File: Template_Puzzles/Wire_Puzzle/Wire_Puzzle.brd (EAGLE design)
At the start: 44.4 x 42.9 mm, 24 parts, among them Q1 2N7002

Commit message: Wire_Puzzle progress
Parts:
- removed J0, J1, J2, J3, J4, J5, J6, J7: (no value), SparkFun-Connectors:1X04
- added D1: 1N4001, Diodes:DO-41
- added IC1: 7805T, linear:TO220H
- added R3: 330R, Resistor:RESAD724W46L381D178B
- added U$10, U$11, U$12, U$13, U$14, U$15, U$16, U$17: 1X02, Adam's Parts (work):1X02
- added U$18, U$19, U$20, U$21, U$22, U$23, U$24, U$25, U$26, U$27: 1X03, Adam's Parts (work):1X03
- FRAME1: value FRAME-LETTER -> FRAME-LEDGER
- Q1: value 2N7002 -> 2N7000
- moved U$9 176.1 mm to (79.0, 47.0)
- moved R2 157.9 mm to (36.0, 58.0), turned to 90 degrees
- moved R1 155.8 mm to (40.4, 58.1), turned to 90 degrees
- moved LED2 150.6 mm to (36.0, 67.0), turned to 270 degrees
- moved LED1 143.9 mm to (17.0, 81.0), turned to 180 degrees
- moved Q1 142.0 mm to (36.0, 50.0), turned to 270 degrees
- moved U$5 139.2 mm to (81.0, 56.0), turned to 90 degrees
- moved U$8 112.8 mm to (8.00, 52.0)
- moved U$4 110.9 mm to (69.0, 43.0), turned to 180 degrees
- moved U$7 105.4 mm to (32.0, 36.0)
- moved U$6 101.1 mm to (23.0, 52.0), turned to 180 degrees
- moved U$2 54.3 mm to (8.01, 79.2), turned to 0 degrees
- moved FRAME1 28.8 mm to (-47.0, -114.0)
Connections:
- new net 3V_1: U$4.P$5
- new net 3V_2: U$4.P$17
- new net 3V_3: U$4.P$26
- new net G_2: U$4.P$6
- new net G_4: U$4.P$18
- new net N$5: LED1.A, R3.2
- new net VU: U$4.P$13
- net 5V: now also D1.C, IC1.3, R3.1, U$18.2, U$19.2, U$20.2, U$21.2, U$22.2, U$23.2, U$24.2, U$25.2, U$26.2, U$27.2
- net A: now also U$10.2; no longer J0.2
- net A0: now also U$27.3
- net B: now also U$11.2; no longer J1.2
- net C: now also U$12.2; no longer J2.2
- net D: now also U$13.2; no longer J3.2
- net D0: now also U$18.3, U$7.2
- net D1: now also U$19.3
- net D2: now also U$20.3, U$3.14; no longer U$7.2
- net D3: now also U$21.3
- net D4: now also U$22.3
- net D5: now also U$23.3
- net D6: now also U$24.3
- net D7: now also U$25.3; no longer U$3.14
- net D8: now also U$26.3
- net E: now also U$14.2; no longer J4.2
- net F: now also U$15.2; no longer J5.2
- net G: now also U$16.2; no longer J6.2
- net GND: now also IC1.2, LED1.K, U$18.1, U$19.1, U$20.1, U$21.1, U$22.1, U$23.1, U$24.1, U$25.1, U$26.1, U$27.1; no longer J0.3, J0.4, J1.3, J1.4, J2.3, J2.4, J3.3, J3.4, J4.3, J4.4, J5.3, J5.4, J6.3, J6.4, J7.3, J7.4
- net H: now also U$17.2; no longer J7.2
- net N$4: now also D1.A
- net QA: now also U$10.1; no longer J0.1
- net QB: now also U$11.1; no longer J1.1
- net QC: now also U$12.1; no longer J2.1
- net QD: now also U$13.1; no longer J3.1
- net QE: now also U$14.1; no longer J4.1
- net QF: now also U$15.1; no longer J5.1
- net QG: now also U$16.1; no longer J6.1
- net QH: now also U$17.1; no longer J7.1
- net VCC: now also IC1.1
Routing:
- net D1: track 0.00 -> 60.1 mm, vias 0 -> 2
- net A0: track 0.00 -> 45.0 mm
- net D8: track 0.00 -> 43.6 mm, vias 0 -> 1
- net D2: track 0.00 -> 36.8 mm
- net N$4: track 0.00 -> 32.3 mm
- net N$1: track 0.00 -> 23.1 mm
- net VCC: track 0.00 -> 19.1 mm
- net D7: track 30.4 -> 47.7 mm, vias 0 -> 1
- net D6: track 21.2 -> 34.4 mm, vias 0 -> 1
- net D3: track 39.5 -> 52.5 mm, vias 0 -> 1
- net N$8: track 0.00 -> 12.7 mm
- net N$3: track 0.00 -> 9.31 mm
- net N$2: track 0.00 -> 9.31 mm
- net 5V: track 17.4 -> 25.3 mm
- net N$7: track 0.00 -> 7.20 mm
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- removed copper zone on layer 1, net GND
- removed copper zone on layer 16, net GND
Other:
- board size 44.4 x 42.9 mm -> 88.4 x 90.8 mm
- board text added: "+"
- board text added: "+12"
- board text added: "A0"
- board text added: "COM"
- board text added: "D0"
- board text added: "D1"
- board text added: "D2"
- board text added: "D3"
- board text added: "D4"
- board text added: "D5"
- board text added: "D6"
- board text added: "D7"
- board text added: "D8"
- board text added: "G 5V S"
- board text added: "NC"
- board text added: "NO"
- board text added: "PUZZLE WIRES"
- board text added: "_"
- board text removed: "5V"
- board text removed: "BTN-"
- board text removed: "LED-"
- board text removed: "WIRE+"
- board text removed: "WIRE-"

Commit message: Progress, added audio amp, power
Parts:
- added C1: 1000uF, adafruit:E5-10,5
- added C2: 100uF, adafruit:E5-10,5
- added C3: 0.1uF, capacitor-wima:C2.5-2
- added C4: 0.33uF, rcl:E2-5
- added C5: 0.1uF, rcl:E2-5
- added D2: 1N4001, Diodes:DO-41
- added R4, R5: 1K, Resistor:RESAD724W46L381D178B
- added R6: 10R, Resistor:RESAD724W46L381D178B
- added S1: (no value), Adam's Parts (work):SWITCH_SLIDING_SSP1S1
- added U1: LM386N, SparkFun-IC-Amplifiers:DIP08
- added VR1: 10k, SparkFun-Resistors:TRIMPOT-PTH-3386U
- R2: value (none) -> 330R
- moved LED1 99.2 mm to (114.0, 60.0), turned to 0 degrees
- moved R3 85.7 mm to (107.8, 63.6), turned to 270 degrees
- moved U$9 73.4 mm to (8.00, 65.7), turned to 180 degrees
- moved IC1 20.6 mm to (27.0, 77.0), turned to 270 degrees
- moved U$2 2.50 mm to (7.99, 76.8), turned to 180 degrees
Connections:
- new net AUDIO: R4.1, R5.1, VR1.2
- new net N$10: C3.2, R6.1
- new net N$11: R5.2, U$5.P$13
- new net N$12: U1.3, VR1.3
- new net N$13: S1.2, U$2.2
- new net N$14: C2.+, U1.7
- new net N$9: C1.-, U$9.1
- net 5V: now also C5.+, D2.A
- net GND: now also C2.-, C4.-, C5.-, R6.2, U$9.2, U1.2, U1.4
- net N$7: now also C1.+, C3.1, U1.5; no longer U$5.P$16, U$9.1
- net N$8: now also R4.2, U$5.P$12; no longer U$5.P$14, U$9.2
- net VCC: now also C4.+, D2.C, S1.3, U1.6; no longer U$2.2
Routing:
- net VCC: track 19.1 -> 0.08 mm
- net N$8: track 12.7 -> 0.00 mm
- net N$4: track 32.3 -> 23.2 mm
- net N$7: track 7.20 -> 0.00 mm
- net 5V: track 25.3 -> 21.8 mm
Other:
- board text added: "SPKR"

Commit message: Finished wire puzzle
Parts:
- R2, R3: value 330R -> 330
- R6: value 10R -> 10
- moved S1 298.2 mm to (9.90, 86.0)
- moved D2 282.0 mm to (14.6, 76.7), turned to 270 degrees
- moved C4 275.5 mm to (19.0, 80.0), turned to 270 degrees
- moved C5 275.5 mm to (19.0, 74.0), turned to 90 degrees
- moved R6 268.4 mm to (51.7, 65.7), turned to 270 degrees
- moved C2 267.0 mm to (49.0, 82.0), turned to 90 degrees
- moved VR1 266.5 mm to (65.0, 84.0)
- moved C3 265.0 mm to (55.1, 65.9), turned to 90 degrees
- moved R5 240.2 mm to (46.0, 67.0), turned to 270 degrees
- moved R4 232.6 mm to (43.0, 67.0), turned to 270 degrees
- moved U1 232.1 mm to (62.1, 65.8), turned to 180 degrees
- moved FRAME1 119.0 mm to (16.0, -13.0)
- moved LED1 94.3 mm to (24.0, 88.0), turned to 180 degrees
- moved R3 73.7 mm to (37.6, 86.2), turned to 180 degrees
- moved U$4 45.2 mm to (41.2, 7.40), turned to 0 degrees
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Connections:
- removed net G_2: U$4.P$6
- removed net G_4: U$4.P$18
- net GND: now also U$4.P$18, U$4.P$6, U$9.1; no longer U$9.2
- net N$9: now also U$9.2; no longer U$9.1
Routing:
- net 5V: track 21.8 -> 183.5 mm, vias 0 -> 2
- net VCC: track 0.08 -> 86.7 mm
- net D0: track 4.48 -> 63.8 mm
- net D2: track 36.8 -> 84.7 mm, vias 0 -> 2
- net D3: track 52.5 -> 96.4 mm, vias 1 -> 3
- net D4: track 33.3 -> 73.3 mm, vias 1 -> 3
- net D5: track 58.3 -> 96.2 mm, vias 0 -> 2
- net N$7: track 0.00 -> 33.3 mm, vias 0 -> 1
- net AUDIO: track 0.00 -> 32.1 mm
- net A0: track 45.0 -> 14.6 mm
- net D1: track 60.1 -> 87.8 mm, vias 2 -> 4
- net D8: track 43.6 -> 71.2 mm, vias 1 -> 3
- net N$14: track 0.00 -> 26.8 mm, vias 0 -> 1
- net D6: track 34.4 -> 60.0 mm, vias 1 -> 3
- net N$12: track 0.00 -> 22.0 mm
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- added copper zone on layer 16, net 5V
- added copper zone on layer 1, net GND
- added copper zone on layer 16, net GND
- added copper zone on layer 16, net N$13
- added copper zone on layer 1, net NOGND
- added copper zone on layer 16, net NOGND
- added copper zone on layer 16, net VCC
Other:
- board size 88.4 x 90.8 mm -> 74.4 x 94.8 mm
- board text added: "D0 - NEOPIXEL D1 - RELAY D2 - SIPO DOUT D3 - PISO LOAD D4 - PISO DIN D5 - SHIFT CLK D6 - SIPO LATCH D7 - DFMINI TX D8 - DFMINI RX A0 - UNUSED"
- board text added: "NEO"
- board text added: "OFF"
- board text added: "ON"
- board text added: "PWR"
- board text added: "RELAY"
- board text removed: "CLK"
- board text removed: "DIN"
- board text removed: "DOUT"
- board text removed: "LATCH"
- board text removed: "LATCH CLK DOUT"
- board text removed: "LOAD"
- board text removed: "LOAD CLK DIN"

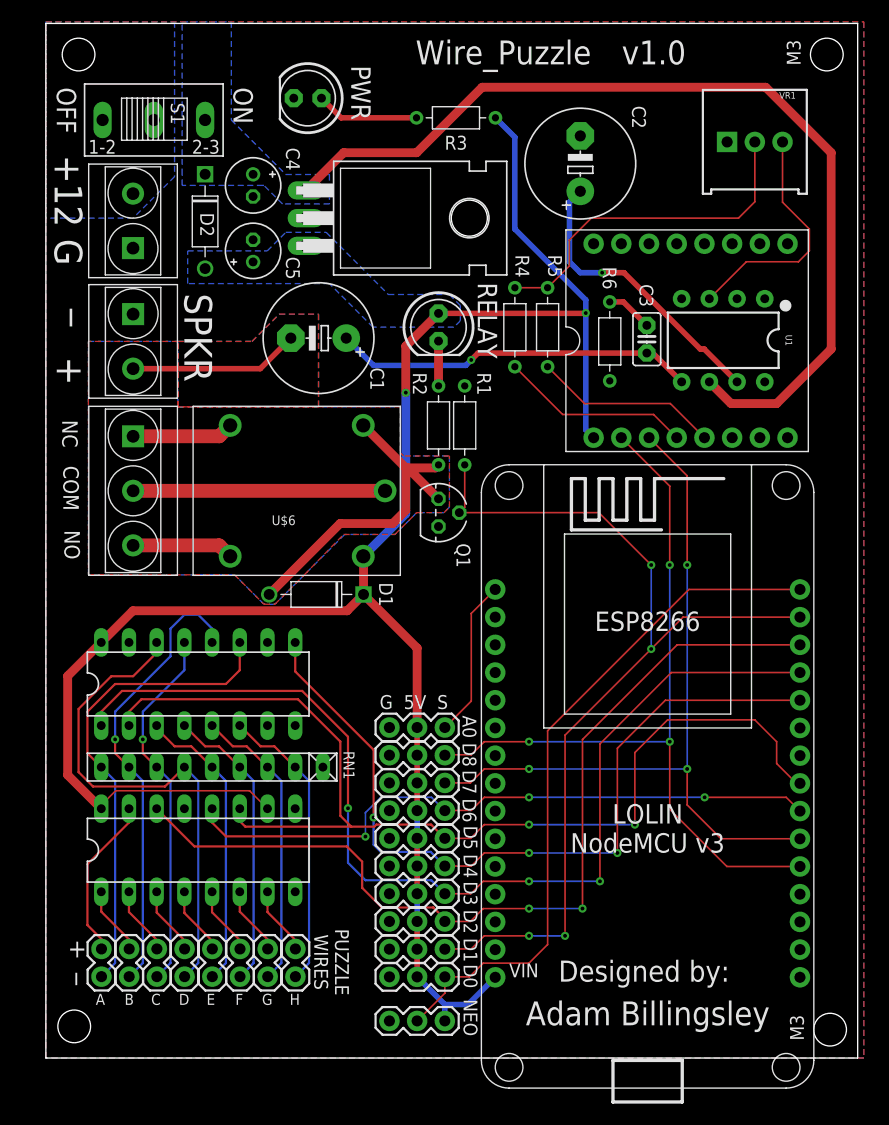
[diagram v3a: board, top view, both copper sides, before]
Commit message: Cleaned up Wire_Puzzle PCB labels, added DC power jack
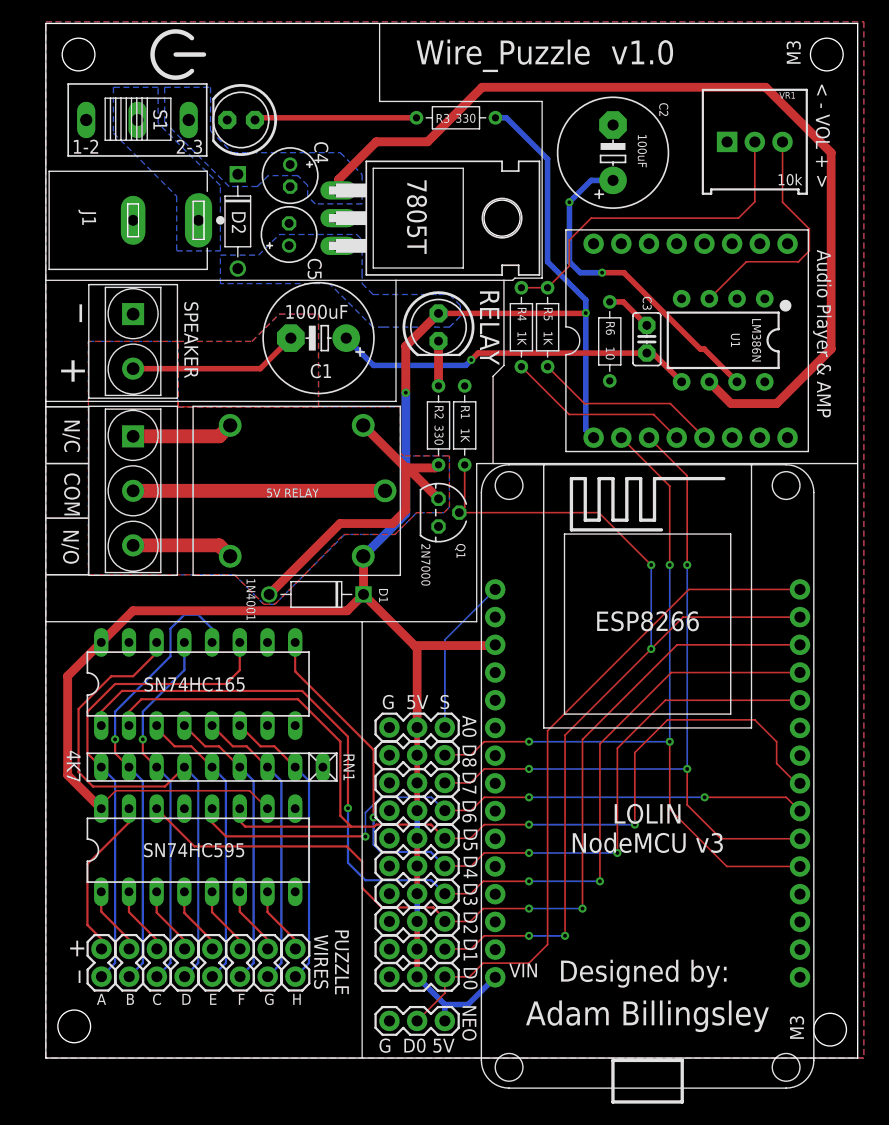
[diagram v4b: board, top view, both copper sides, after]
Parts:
- removed U$2: TERMINAL_BLOCK_2P, Adam's Parts (work):H2-5.0-10.5X8.0MM
- added J1: POWER_JACK_PJ-037A, Adam's Parts (work):CUI_PJ-037A
- moved LED1 6.42 mm to (17.9, 86.0)
- moved C5 3.62 mm to (22.3, 75.5)
- moved C4 3.52 mm to (22.4, 80.9)
- moved C2 3.16 mm to (52.0, 83.0)
- moved D2 3.00 mm to (17.6, 76.7)
- moved IC1 3.00 mm to (37.0, 77.0)
- moved S1 1.50 mm to (8.40, 86.0)
- moved R4 0.60 mm to (43.6, 67.0)
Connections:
- removed net VU: U$4.P$13
- net 5V: now also U$4.P$13
- net GND: now also J1.2; no longer U$2.1
- net N$13: now also J1.1; no longer U$2.2
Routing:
- net 5V: track 183.5 -> 191.5 mm
- net N$5: track 9.46 -> 14.9 mm
- net N$14: track 26.8 -> 30.2 mm, vias 1 -> 2
- net VCC: track 86.7 -> 84.3 mm
- net N$8: track 17.5 -> 16.9 mm
- net AUDIO: track 32.1 -> 31.5 mm
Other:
- board text added: "5V RELAY"
- board text added: "< - VOL + >"
- board text added: "Audio Player & AMP"
- board text added: "G D0 5V"
- board text added: "N/C"
- board text added: "N/O"
- board text added: "SPEAKER"
- board text removed: "+12"
- board text removed: "NC"
- board text removed: "NO"
- board text removed: "OFF"
- board text removed: "ON"
- board text removed: "PWR"
- board text removed: "SPKR"
